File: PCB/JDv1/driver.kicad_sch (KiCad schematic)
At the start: 0 parts

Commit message: started adding Typical Application to DRV8302 Driver stage
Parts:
- added C1: 0.015u, symbol Device:C_Small
- added C2: 120p, symbol Device:C_Small
- added C3: 6800p, symbol Device:C_Small
- added C4: 0.022u, symbol Device:C_Small
- added C5: 2.2u, symbol Device:C_Small
- added C6, C7: 1u, symbol Device:C_Small
- added C8, C9: 2200p, symbol Device:C_Small
- added IC1: DRV8302, DRV8302:TSSOP-56_3, symbol JobotSymbols:DRV8302
- added R1: 205k, symbol Device:R_Small_US
- added R10, R9: 56, symbol Device:R_Small_US
- added R2: 16.2k, symbol Device:R_Small_US
- added R3: 31.6k, symbol Device:R_Small_US
- added R4, R5, R6, R7: 10k, symbol Device:R_Small_US
- added R8: 1, symbol Device:R_Small_US
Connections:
- new net: C7.2, IC1.27 (AVDD)
- new net: IC1.1 (RT_CLK), R1.1
- new net: IC1.7 (DTC), R8.1
- new net: C4.1, IC1.15 (CP2)
- new net: C4.2, IC1.14 (CP1)
- new net: C6.2, IC1.23 (DVDD)
- new net: C3.1, R2.2
- new net: IC1.3 (VSENSE), R3.2, R4.1
- new net: C2.1, IC1.2 (COMP), R2.1
- new net: C5.1, IC1.13 (GVDD)
- new net: IC1.25 (SO1), R9.1
- new net: IC1.26 (SO2), R10.1
- new net: IC1.50 (PH), IC1.51 (PH)
- new net: IC1.53 (PVDD2), IC1.54 (PVDD2)
- new net: C1.1, IC1.56 (SS_TR)
- new net DC_CAL: IC1.12 (DC_CAL)
- new net EN_GATE: IC1.16 (EN_GATE)
- new net GAIN: IC1.10 (GAIN)
- new net GND: C1.2, C2.2, C3.2, C5.2, C8.1, C9.1, R1.2, R8.2
- new net GNDA: C6.1, C7.1, IC1.28 (AGND), IC1.57 (AGND), IC1.58 (AGND), IC1.59 (AGND)
- new net INH_A: IC1.17 (INH_A)
- new net INH_B: IC1.19 (INH_B)
- new net INH_C: IC1.21 (INH_C)
- new net INL_A: IC1.18 (INL_A)
- new net INL_B: IC1.20 (INL_B)
- new net INL_C: IC1.22 (INL_C)
- new net M_OC: IC1.9 (M_OC)
- new net M_PWM: IC1.8 (M_PWM)
- new net OC_ADJ: IC1.11 (OC_ADJ)
- new net PWRGD: IC1.4 (PWRGD), R5.2
- new net REF: IC1.24 (REF)
- new net SO1: R9.2
- new net SO2: C8.2, C9.2, R10.2
- new net VLOGIC: R3.1, R5.1, R6.1, R7.1
- new net nFAULT: IC1.6 (~{FAULT}), R7.2
- new net nOCTW: IC1.5 (~{OCTW}), R6.2
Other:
- title: (none) -> Driver

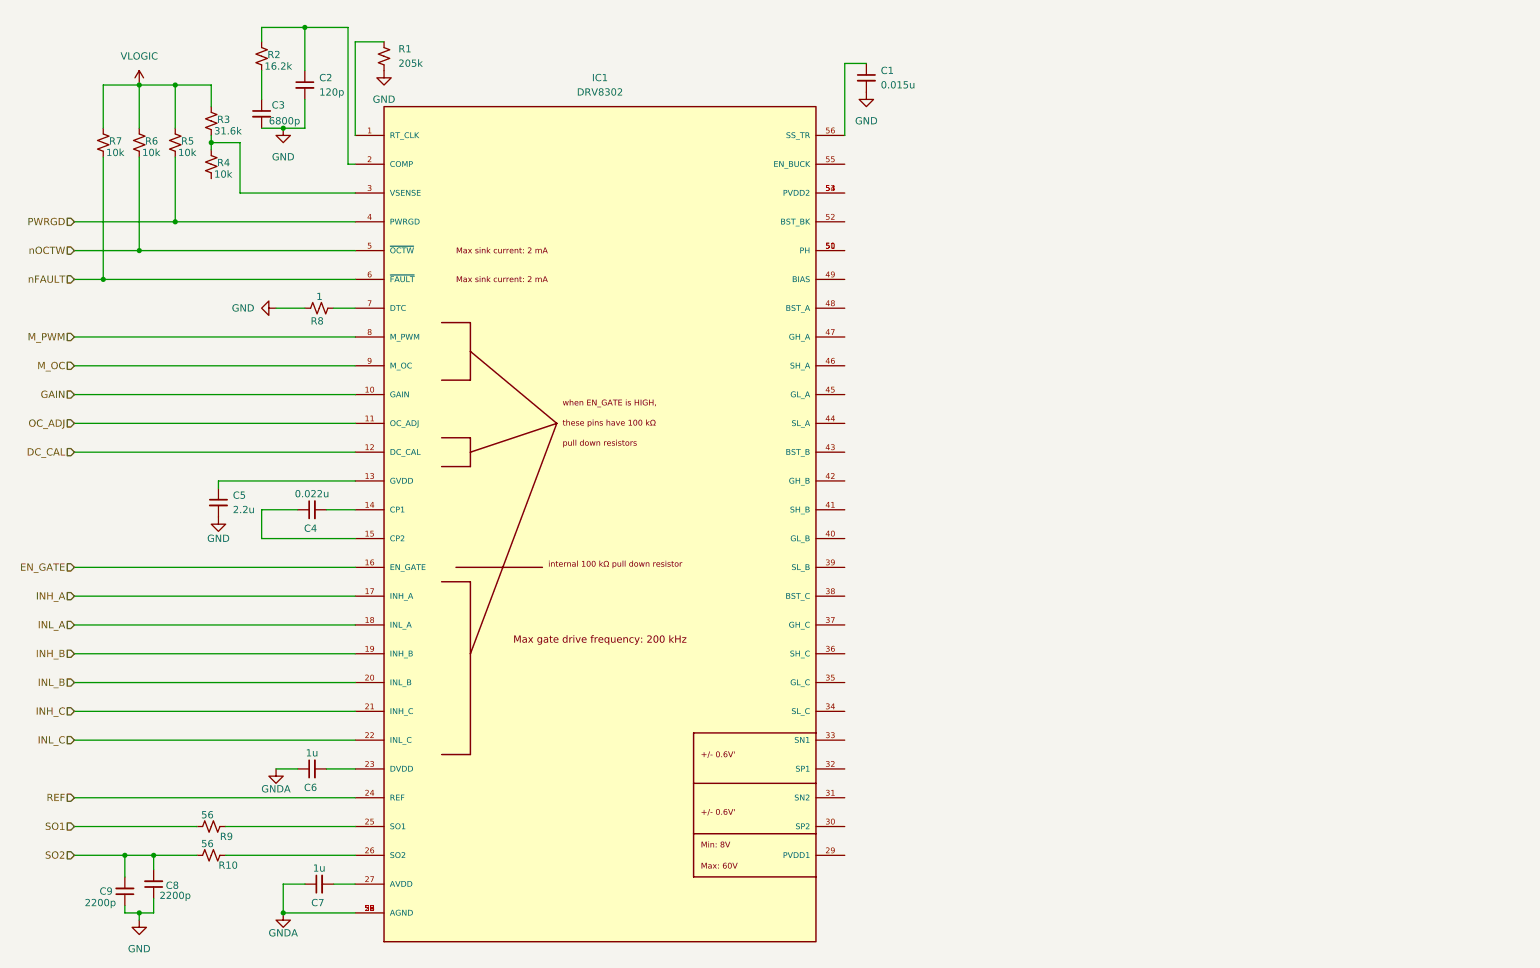
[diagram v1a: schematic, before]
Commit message: added more from DRV8302 Typical Application
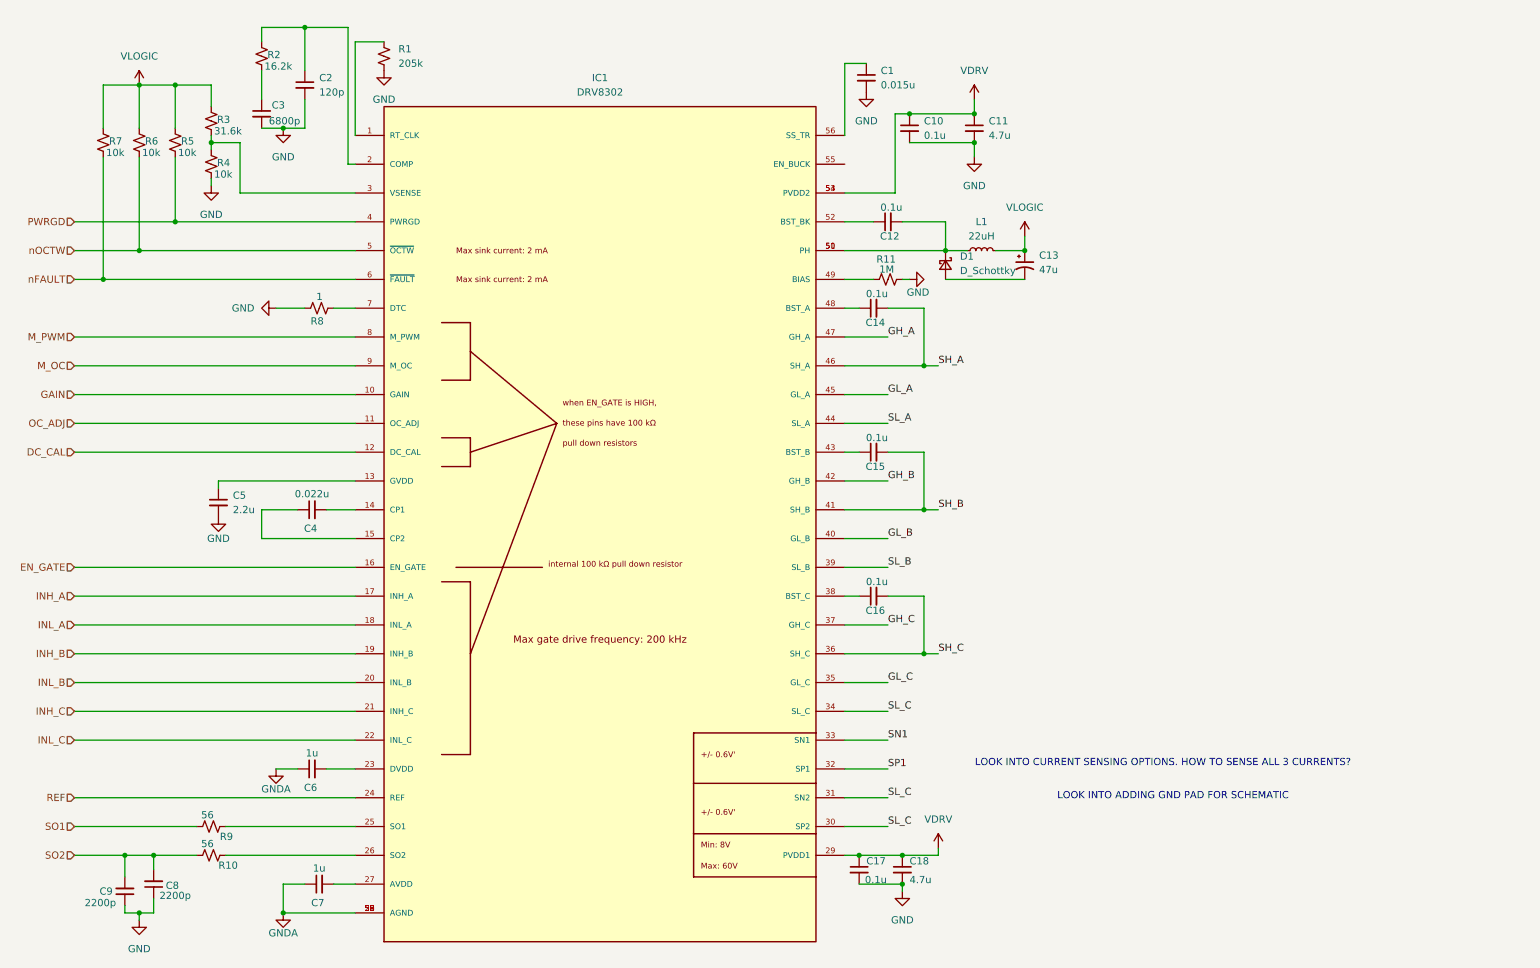
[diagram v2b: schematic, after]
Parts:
- added C10, C12, C14, C15, C16, C17: 0.1u, symbol Device:C_Small
- added C11, C18: 4.7u, symbol Device:C_Small
- added C13: 47u, symbol Device:C_Polarized_Small_US
- added D1: D_Schottky, symbol Device:D_Schottky_Small
- added L1: 22uH, symbol Device:L_Small
- added R11: 1M, symbol Device:R_Small_US
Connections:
- net GND: now also R4.2, C10.2, C11.2, C17.2, C18.2, R11.1
- net VLOGIC: now also C13.1, L1.2
- net VDRV: now reaches IC1.29 (PVDD1)
- net VDRV: now also IC1.53 (PVDD2), IC1.54 (PVDD2), C10.1, C11.1, C17.1, C18.1
- net SL_C: now reaches IC1.30 (SP2)
- net SL_C: now also IC1.31 (SN2), IC1.34 (SL_C)
- net SP1: now reaches IC1.32 (SP1)
- net SN1: now reaches IC1.33 (SN1)
- net GL_C: now reaches IC1.35 (GL_C)
- net SH_C: now reaches IC1.36 (SH_C)
- net SH_C: now also C16.2
- net GH_C: now reaches IC1.37 (GH_C)
- net at IC1.38 (BST_C): now also C16.1
- net SL_B: now reaches IC1.39 (SL_B)
- net GL_B: now reaches IC1.40 (GL_B)
- net SH_B: now reaches IC1.41 (SH_B)
- net SH_B: now also C15.2
- net GH_B: now reaches IC1.42 (GH_B)
- net at IC1.43 (BST_B): now also C15.1
- net SL_A: now reaches IC1.44 (SL_A)
- net GL_A: now reaches IC1.45 (GL_A)
- net SH_A: now reaches IC1.46 (SH_A)
- net SH_A: now also C14.2
- net GH_A: now reaches IC1.47 (GH_A)
- net at IC1.48 (BST_A): now also C14.1
- net at IC1.49 (BIAS): now also R11.2
- net at IC1.50 (PH), IC1.51 (PH): now also C12.2, D1.1 (K), L1.1
- net at IC1.52 (BST_BK): now also C12.1
- new net: C13.2, D1.2 (A)
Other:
- note added: "LOOK INTO ADDING GND PAD FOR SCHEMATIC"
- note added: "LOOK INTO CURRENT SENSING OPTIONS. HOW TO SENSE ALL 3 CURRENTS?"

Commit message: added driver with half driver hierarchical pages
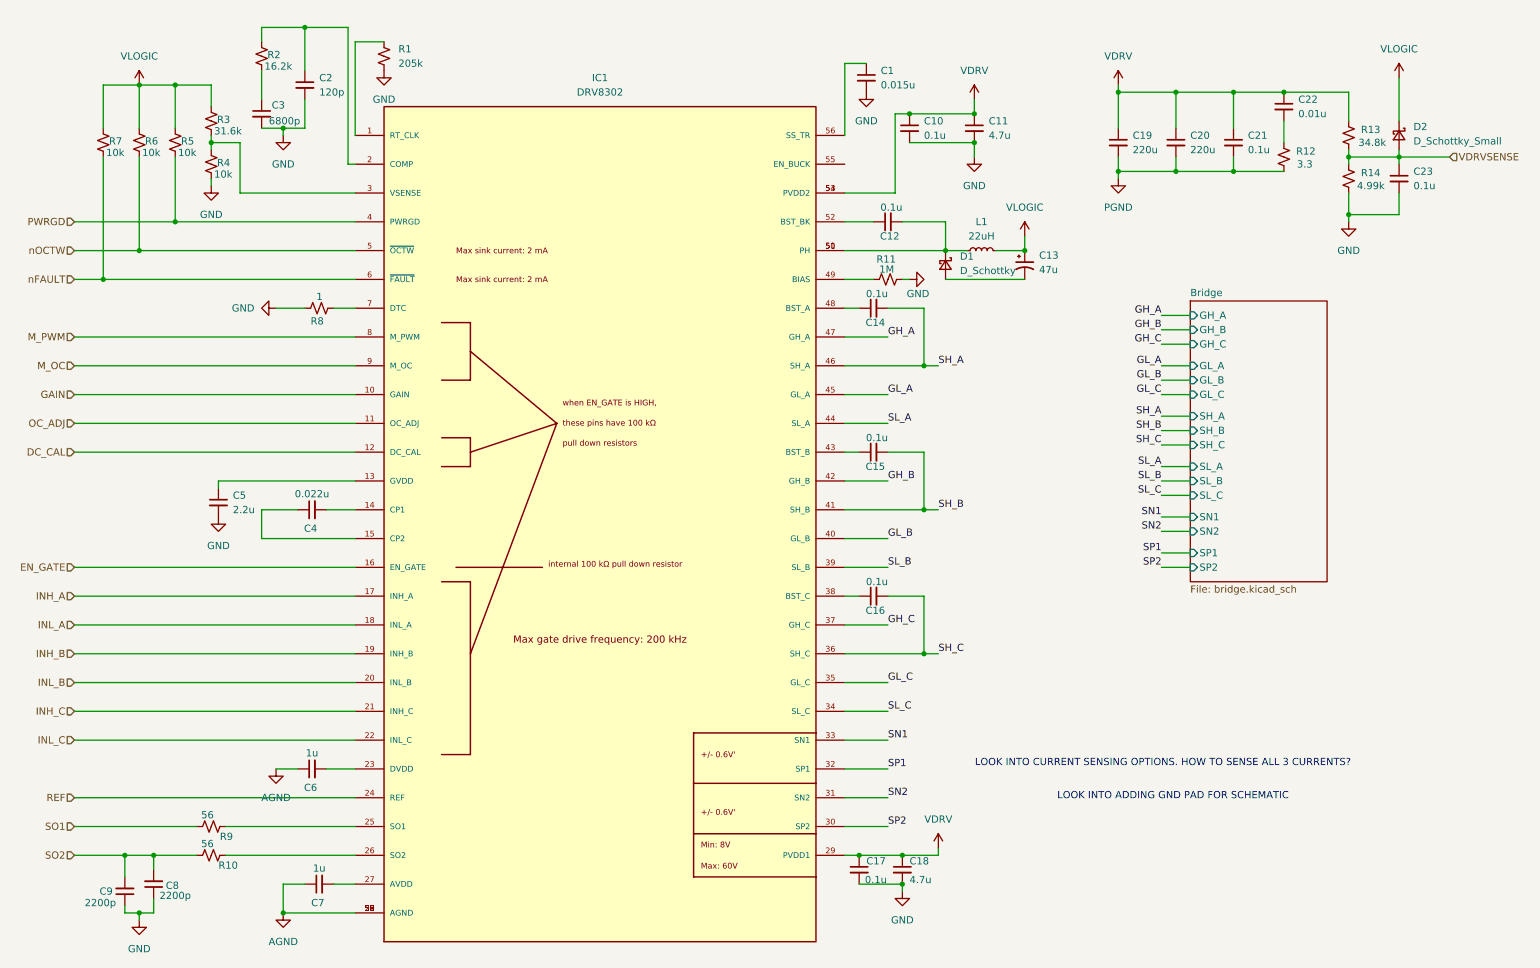
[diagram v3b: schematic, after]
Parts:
- added C19, C20: 220u, symbol Device:C_Small
- added C21, C23: 0.1u, symbol Device:C_Small
- added C22: 0.01u, symbol Device:C_Small
- added D2: D_Schottky_Small, symbol Device:D_Schottky_Small
- added R12: 3.3, symbol Device:R_Small_US
- added R13: 34.8k, symbol Device:R_Small_US
- added R14: 4.99k, symbol Device:R_Small_US
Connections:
- net GND: now also C23.2, R14.1
- net SL_C: no longer IC1.30 (SP2), IC1.31 (SN2)
- net VDRV: now also C19.1, C20.1, C21.1, C22.1, R13.2
- net VLOGIC: now also D2.1 (K)
- net GNDA renamed AGND
- new net: C22.2, R12.2
- new net PGND: C19.2, C20.2, C21.2, R12.1
- new net SN2: IC1.31 (SN2)
- new net SP2: IC1.30 (SP2)
- new net VDRVSENSE: C23.1, D2.2 (A), R13.1, R14.2
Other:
- added sheet Bridge (bridge.kicad_sch)

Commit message: syncing
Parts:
- C1, C10, C11, C12, C13, C14, C15, C16, C17, C18, C19, C2, C20, C21, C22, C23, C3, C4, C5, C6, C7, C8, C9: footprint (none) -> Capacitor_SMD:C_0603_1608Metric
- D1: value D_Schottky -> D_Schottky_Small; footprint (none) -> Diode_SMD:D_SMA
- D2: footprint (none) -> Diode_SMD:D_SMA
- L1: footprint (none) -> Inductor_SMD:L_0603_1608Metric
- R1, R10, R11, R12, R13, R14, R2, R3, R4, R5, R6, R7, R8, R9: footprint (none) -> Resistor_SMD:R_0603_1608Metric
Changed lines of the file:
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@@
 			)
 		)
-		(property "Footprint" ""
+		(property "Footprint" "Capacitor_SMD:C_0603_1608Metric"
 			(at 167.64 53.34 0)
 			(effects
@@
 			)
 		)
-		(property "Footprint" ""
+		(property "Footprint" "Capacitor_SMD:C_0603_1608Metric"
 			(at 67.31 170.18 0)
 			(effects
@@
 			)
 		)
-		(property "Footprint" ""
+		(property "Footprint" "Capacitor_SMD:C_0603_1608Metric"
 			(at 182.88 36.83 0)
 			(effects
@@
 			)
 		)
-		(property "Footprint" ""
+		(property "Footprint" "Resistor_SMD:R_0603_1608Metric"
 			(at 248.92 38.1 0)
 			(effects
@@
 			)
 		)
-		(property "Footprint" ""
+		(property "Footprint" "Inductor_SMD:L_0603_1608Metric"
 			(at 184.15 58.42 0)
 			(effects
@@
 			)
 		)
-		(property "Footprint" ""
+		(property "Footprint" "Capacitor_SMD:C_0603_1608Metric"
 			(at 191.77 60.96 0)
 			(effects
@@
 			)
 		)
-		(property "Footprint" ""
+		(property "Footprint" "Resistor_SMD:R_0603_1608Metric"
 			(at 78.74 24.13 0)
 			(effects
@@
 			)
 		)
-		(property "Footprint" ""
+		(property "Footprint" "Resistor_SMD:R_0603_1608Metric"
 			(at 167.64 63.5 0)
 			(effects
@@
 			)
 		)
-		(property "Footprint" ""
+		(property "Footprint" "Capacitor_SMD:C_0603_1608Metric"
 			(at 218.44 39.37 0)
 			(effects
@@
 			)
 		)
-		(property "Footprint" ""
+		(property "Footprint" "Resistor_SMD:R_0603_1608Metric"
 			(at 67.31 68.58 0)
 			(effects
@@
 			)
 		)
-		(property "Footprint" ""
+		(property "Footprint" "Resistor_SMD:R_0603_1608Metric"
 			(at 35.56 39.37 0)
 			(effects
@@
 			)
 		)
-		(property "Footprint" ""
+		(property "Footprint" "Capacitor_SMD:C_0603_1608Metric"
 			(at 38.1 170.18 0)
 			(effects
@@
 			)
 		)
-		(property "Footprint" ""
+		(property "Footprint" "Capacitor_SMD:C_0603_1608Metric"
 			(at 66.04 104.14 0)
 			(effects
@@
 			)
 		)
-		(property "Footprint" ""
+		(property "Footprint" "Capacitor_SMD:C_0603_1608Metric"
 			(at 237.49 33.02 0)
 			(effects
@@
 			)
 		)
-		(property "Footprint" ""
+		(property "Footprint" "Capacitor_SMD:C_0603_1608Metric"
 			(at 66.04 149.86 0)
 			(effects
@@
 	)
 	(symbol
+		(lib_id "Device:D_Schottky_Small")
+		(at 177.8 60.96 270)
+		(unit 1)
+		(exclude_from_sim no)
+		(in_bom yes)
+		(on_board yes)
+		(dnp no)
+		(fields_autoplaced yes)
+		(property "Reference" "D1"
+			(at 180.34 59.4359 90)
+			(effects
+				(font
+					(size 1.27 1.27)
+				)
+				(justify left)
+			)
+		)
+		(property "Value" "D_Schottky_Small"
+			(at 180.34 61.9759 90)
+			(effects
+				(font
+					(size 1.27 1.27)
+				)
+				(justify left)
+			)
+		)
+		(property "Footprint" "Diode_SMD:D_SMA"
+			(at 177.8 60.96 90)
+			(effects
+				(font
+					(size 1.27 1.27)
+				)
+				(hide yes)
+			)
+		)
+		(property "Datasheet" "~"
+			(at 177.8 60.96 90)
+			(effects
+				(font
+					(size 1.27 1.27)
+				)
+				(hide yes)
+			)
+		)
+		(property "Description" "Schottky diode, small symbol"
+			(at 177.8 60.96 0)
+			(effects
+				(font
+					(size 1.27 1.27)
+				)
+				(hide yes)
+			)
+		)
+		(pin "1"
+		)
+		(pin "2"
+		)
+		(instances
+			(project "JDv1"
+				(path "/34add074-477f-4875-915d-3320ca70c4f4/99cc1ace-a3d0-4c8e-ae28-91c04f5cfd08"
+					(reference "D1")
+					(unit 1)
+				)
+			)
+		)
+	)
+	(symbol
 		(lib_id "Device:C_Small")
 		(at 57.15 34.29 0)
@@
 			)
 		)
-		(property "Footprint" ""
+		(property "Footprint" "Capacitor_SMD:C_0603_1608Metric"
 			(at 57.15 34.29 0)
 			(effects
@@
 			)
 		)
-		(property "Footprint" ""
+		(property "Footprint" "Resistor_SMD:R_0603_1608Metric"
 			(at 48.26 35.56 0)
 			(effects
@@
 			)
 		)
-		(property "Footprint" ""
+		(property "Footprint" "Resistor_SMD:R_0603_1608Metric"
 			(at 57.15 24.13 0)
 			(effects
@@
 			)
 		)
-		(property "Footprint" ""
+		(property "Footprint" "Capacitor_SMD:C_0603_1608Metric"
 			(at 64.77 29.21 0)
 			(effects
@@
 			)
 		)
-		(property "Footprint" ""
+		(property "Footprint" "Capacitor_SMD:C_0603_1608Metric"
 			(at 162.56 167.64 0)
 			(effects
@@
 			)
 		)
-		(property "Footprint" ""
+		(property "Footprint" "Capacitor_SMD:C_0603_1608Metric"
 			(at 165.1 93.98 0)
 			(effects
@@
 			)
 		)
-		(property "Footprint" ""
+		(property "Footprint" "Capacitor_SMD:C_0603_1608Metric"
 			(at 170.18 167.64 0)
 			(effects
@@
 			)
 		)
-		(property "Footprint" ""
+		(property "Footprint" "Resistor_SMD:R_0603_1608Metric"
 			(at 48.26 43.18 0)
 			(effects
@@
 			)
 		)
-		(property "Footprint" ""
+		(property "Footprint" "Capacitor_SMD:C_0603_1608Metric"
 			(at 257.81 45.72 0)
 			(effects
@@
 			)
 		)
-		(property "Footprint" ""
+		(property "Footprint" "Diode_SMD:D_SMA"
 			(at 257.81 38.1 90)
 			(effects
@@
 	)
 	(symbol
-		(lib_id "Device:D_Schottky_Small")
-		(at 177.8 60.96 270)
-		(unit 1)
-		(exclude_from_sim no)
-		(in_bom yes)
-		(on_board yes)
-		(dnp no)
-		(fields_autoplaced yes)
-		(property "Reference" "D1"
-			(at 180.34 59.4359 90)
-			(effects
-				(font
-					(size 1.27 1.27)
-				)
-				(justify left)
-			)
-		)
-		(property "Value" "D_Schottky"
-			(at 180.34 61.9759 90)
-			(effects
-				(font
-					(size 1.27 1.27)
-				)
-				(justify left)
-			)
-		)
-		(property "Footprint" ""
-			(at 177.8 60.96 90)
-			(effects
-				(font
-					(size 1.27 1.27)
-				)
-				(hide yes)
-			)
-		)
-		(property "Datasheet" "~"
-			(at 177.8 60.96 90)
-			(effects
-				(font
-					(size 1.27 1.27)
-				)
-				(hide yes)
-			)
-		)
-		(property "Description" "Schottky diode, small symbol"
-			(at 177.8 60.96 0)
-			(effects
-				(font
-					(size 1.27 1.27)
-				)
-				(hide yes)
-			)
-		)
-		(pin "2"
-		)
-		(pin "1"
-		)
-		(instances
-			(project ""
-				(path "/34add074-477f-4875-915d-3320ca70c4f4/99cc1ace-a3d0-4c8e-ae28-91c04f5cfd08"
-					(reference "D1")
-					(unit 1)
-				)
-			)
-		)
-	)
-	(symbol
 		(lib_id "Device:C_Small")
 		(at 49.53 102.87 0)
@@
 			)
 		)
-		(property "Footprint" ""
+		(property "Footprint" "Capacitor_SMD:C_0603_1608Metric"
 			(at 49.53 102.87 0)
 			(effects
@@
 			)
 		)
-		(property "Footprint" ""
+		(property "Footprint" "Capacitor_SMD:C_0603_1608Metric"
 			(at 171.45 36.83 0)
 			(effects
@@
 			)
 		)
-		(property "Footprint" ""
+		(property "Footprint" "Resistor_SMD:R_0603_1608Metric"
 			(at 48.26 160.02 0)
 			(effects
@@
 			)
 		)
-		(property "Footprint" ""
+		(property "Footprint" "Capacitor_SMD:C_0603_1608Metric"
 			(at 228.6 39.37 0)
 			(effects
@@
 			)
 		)
-		(property "Footprint" ""
+		(property "Footprint" "Capacitor_SMD:C_0603_1608Metric"
 			(at 165.1 119.38 0)
 			(effects
@@
 			)
 		)
-		(property "Footprint" ""
+		(property "Footprint" "Resistor_SMD:R_0603_1608Metric"
 			(at 48.26 165.1 0)
 			(effects
@@
 			)
 		)
-		(property "Footprint" ""
+		(property "Footprint" "Resistor_SMD:R_0603_1608Metric"
 			(at 248.92 45.72 0)
 			(effects
@@
 			)
 		)
-		(property "Footprint" ""
+		(property "Footprint" "Resistor_SMD:R_0603_1608Metric"
 			(at 237.49 41.91 0)
 			(effects
@@
 			)
 		)
-		(property "Footprint" ""
+		(property "Footprint" "Resistor_SMD:R_0603_1608Metric"
 			(at 29.21 39.37 0)
 			(effects
@@
 			)
 		)
-		(property "Footprint" ""
+		(property "Footprint" "Capacitor_SMD:C_0603_1608Metric"
 			(at 33.02 171.45 0)
 			(effects
@@
 			)
 		)
-		(property "Footprint" ""
+		(property "Footprint" "Capacitor_SMD:C_0603_1608Metric"
 			(at 165.1 68.58 0)
 			(effects
@@
 			)
 		)
-		(property "Footprint" ""
+		(property "Footprint" "Resistor_SMD:R_0603_1608Metric"
 			(at 41.91 39.37 0)
 			(effects
@@
 			)
 		)
-		(property "Footprint" ""
+		(property "Footprint" "Capacitor_SMD:C_0603_1608Metric"
 			(at 163.83 27.94 0)
 			(effects
@@
 			)
 		)
-		(property "Footprint" ""
+		(property "Footprint" "Capacitor_SMD:C_0603_1608Metric"
 			(at 208.28 39.37 0)
 			(effects

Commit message: initialized test branch
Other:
- note added: "TEST TO USE INDIVIDUAL GATE DRIVERS INSTEAD OF DRV8302 WILL PREVENT LIMITING FEATURES (e.g. 2-phase inline vs 3-phase)"
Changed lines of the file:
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@@
 		(date "2025-07-27")
+	)
+	(text "TEST TO USE INDIVIDUAL GATE DRIVERS INSTEAD OF DRV8302\nWILL PREVENT LIMITING FEATURES (e.g. 2-phase inline vs 3-phase)"
+		(exclude_from_sim no)
+		(at 138.684 18.796 0)
+		(effects
+			(font
+				(size 1.27 1.27)
+			)
+		)
 	)
 	(text "LOOK INTO CURRENT SENSING OPTIONS. HOW TO SENSE ALL 3 CURRENTS?"
